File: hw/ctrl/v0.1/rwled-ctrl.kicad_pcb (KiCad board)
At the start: 2 copper layers, 70.9 x 38.1 mm, 49 parts, among them J21 batt-chg, J31 USB_B_Micro, J61 led-a, J62 led-b, J63 led-c, J64 led-d, J65 batt-ab, J66 batt-cd, Q31 UMH3N, Q61 IRF4905STRLPBF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

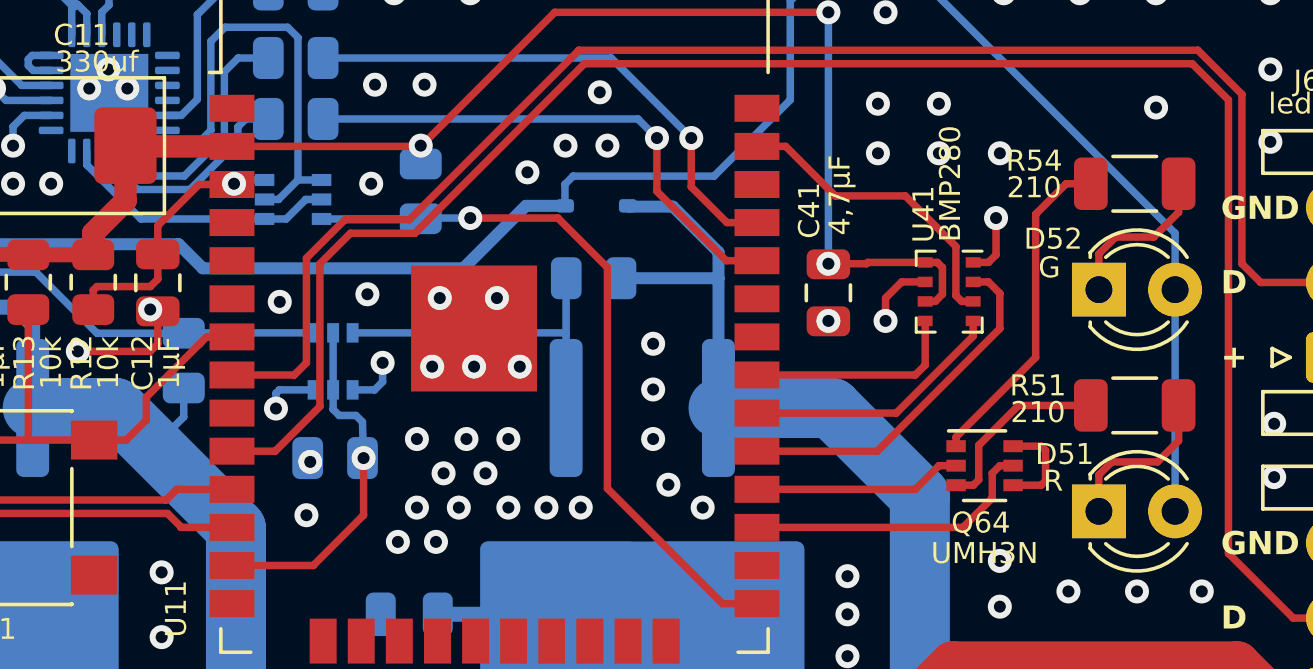
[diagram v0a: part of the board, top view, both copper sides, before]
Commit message: hw - архив доработанных и отправленных в заказ плат
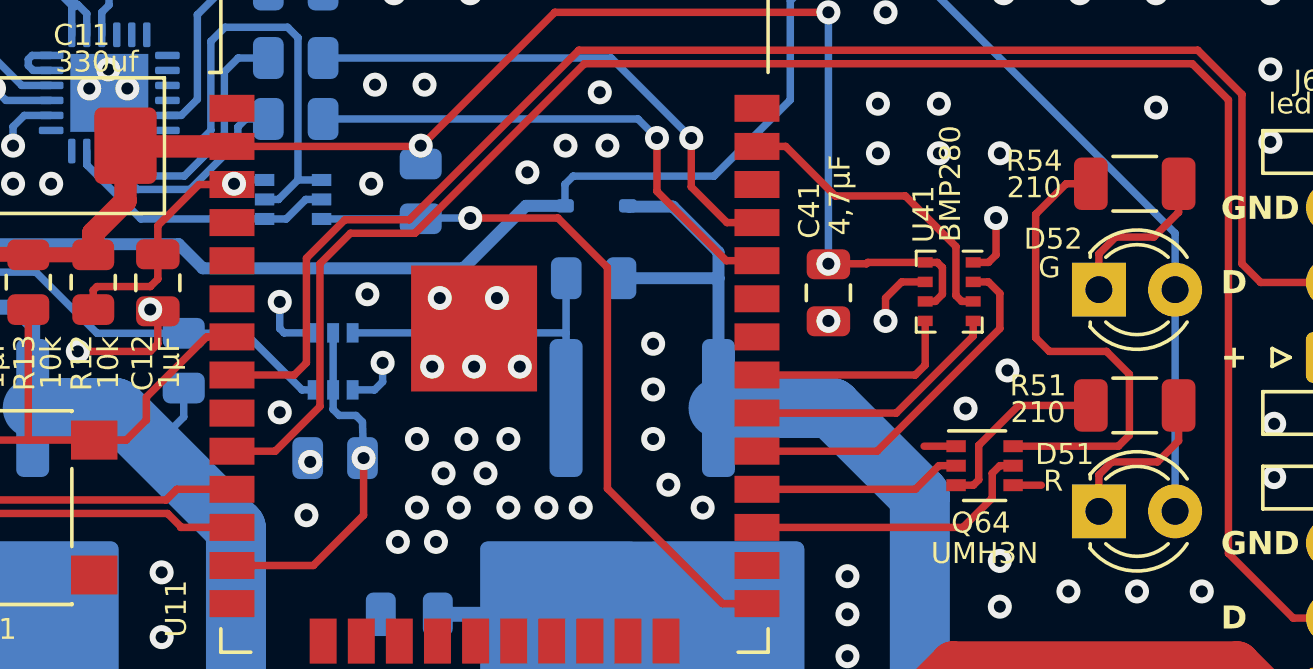
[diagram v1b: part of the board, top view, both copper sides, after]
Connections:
- Q63 pad 1: Net-(Q61-G) -> GND
- Q63 pad 6: GND -> Net-(Q61-G)
- Q64 pad 1: Net-(Q64A-E1) -> GND
- Q64 pad 6: GND -> Net-(Q64A-C1)
- R54 pad 1: Net-(Q64A-E1) -> Net-(Q64A-C1)
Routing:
- net Net-(Q64A-C1): track 0.00 -> 16.1 mm
- net Net-(Q64A-E1): track 11.1 -> 0.00 mm
- net GND: track 41.0 -> 40.0 mm, vias 156 -> 158
- net Net-(Q61-G): track 19.0 -> 19.8 mm
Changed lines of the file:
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@@
   (net 68 "unconnected-(U31-~{DCD}-Pad24)")
   (net 69 "Net-(Q62-G)")
-  (net 70 "Net-(Q64A-E1)")
+  (net 70 "Net-(Q64A-C1)")
   (net 71 "Net-(Q64B-C2)")
   (footprint "Resistor_SMD:R_0805_2012Metric" (layer "F.Cu")
@@
       (stroke (width 0.1) (type solid)) (layer "F.Fab"))
     (pad "1" smd rect (at -0.95 -0.65) (size 0.65 0.4) (layers "F.Cu" "F.Paste" "F.Mask")
-      (net 70 "Net-(Q64A-E1)") (pinfunction "E1") (pintype "passive"))
+      (net 2 "GND") (pinfunction "E1") (pintype "passive"))
     (pad "2" smd rect (at -0.95 0) (size 0.65 0.4) (layers "F.Cu" "F.Paste" "F.Mask")
       (net 30 "/led-g") (pinfunction "B1") (pintype "input"))
@@
       (net 29 "/led-r") (pinfunction "B2") (pintype "input"))
     (pad "6" smd rect (at 0.95 -0.65) (size 0.65 0.4) (layers "F.Cu" "F.Paste" "F.Mask")
-      (net 2 "GND") (pinfunction "C1") (pintype "passive"))
+      (net 70 "Net-(Q64A-C1)") (pinfunction "C1") (pintype "passive"))
     (model "${KICAD6_3DMODEL_DIR}/Package_TO_SOT_SMD.3dshapes/SOT-363_SC-70-6.wrl"
       (offset (xyz 0 0 0))
@@
       (stroke (width 0.1) (type solid)) (layer "F.Fab"))
     (pad "1" smd roundrect (at -1.4625 0) (size 1.125 1.75) (layers "F.Cu" "F.Paste" "F.Mask") (roundrect_rratio 0.2222222222)
-      (net 70 "Net-(Q64A-E1)") (pintype "passive"))
+      (net 70 "Net-(Q64A-C1)") (pintype "passive"))
     (pad "2" smd roundrect (at 1.4625 0) (size 1.125 1.75) (layers "F.Cu" "F.Paste" "F.Mask") (roundrect_rratio 0.2222222222)
       (net 10 "Net-(D52-K)") (pintype "passive"))
@@
       (stroke (width 0.1) (type solid)) (layer "B.Fab"))
     (pad "1" smd rect (at -0.95 0.65 270) (size 0.65 0.4) (layers "B.Cu" "B.Paste" "B.Mask")
-      (net 21 "Net-(Q61-G)") (pinfunction "E1") (pintype "passive"))
+      (net 2 "GND") (pinfunction "E1") (pintype "passive"))
     (pad "2" smd rect (at -0.95 0 270) (size 0.65 0.4) (layers "B.Cu" "B.Paste" "B.Mask")
       (net 31 "leden") (pinfunction "B1") (pintype "input"))
@@
       (net 31 "leden") (pinfunction "B2") (pintype "input"))
     (pad "6" smd rect (at 0.95 0.65 270) (size 0.65 0.4) (layers "B.Cu" "B.Paste" "B.Mask")
-      (net 2 "GND") (pinfunction "C1") (pintype "passive"))
+      (net 21 "Net-(Q61-G)") (pinfunction "C1") (pintype "passive"))
     (model "${KICAD6_3DMODEL_DIR}/Package_TO_SOT_SMD.3dshapes/SOT-363_SC-70-6.wrl"
       (offset (xyz 0 0 0))
@@
   (segment (start 128.016 57.404) (end 128.016 56.322) (width 0.25) (layer "F.Cu") (net 2))
   (segment (start 141.7104 76.835) (end 138.303 76.835) (width 1) (layer "F.Cu") (net 2))
-  (segment (start 157.607 60.96) (end 157.607 61.976) (width 0.25) (layer "F.Cu") (net 2))
   (segment (start 152.273 55.88) (end 152.273 56.642) (width 0.25) (layer "F.Cu") (net 2))
   (segment (start 155.194 54.692) (end 155.702 54.692) (width 0.25) (layer "F.Cu") (net 2))
-  (segment (start 157.607 61.976) (end 157.465 62.118) (width 0.25) (layer "F.Cu") (net 2))
   (segment (start 125.643 76.835) (end 122.555 76.835) (width 1) (layer "F.Cu") (net 2))
-  (segment (start 157.465 60.818) (end 157.607 60.96) (width 0.25) (layer "F.Cu") (net 2))
   (segment (start 115.738 46.134) (end 115.738 47.711) (width 0.4) (layer "F.Cu") (net 2))
   (segment (start 125.349 57.658) (end 127.762 57.658) (width 0.25) (layer "F.Cu") (net 2))
   (segment (start 155.956 53.213) (end 155.956 54.438) (width 0.25) (layer "F.Cu") (net 2))
   (segment (start 155.956 54.438) (end 155.702 54.692) (width 0.25) (layer "F.Cu") (net 2))
-  (segment (start 156.525 60.818) (end 157.465 60.818) (width 0.25) (layer "F.Cu") (net 2))
+  (segment (start 154.625 60.818) (end 153.558 60.818) (width 0.25) (layer "F.Cu") (net 2))
   (segment (start 152.811 55.342) (end 152.273 55.88) (width 0.25) (layer "F.Cu") (net 2))
   (segment (start 127.762 57.658) (end 128.016 57.404) (width 0.25) (layer "F.Cu") (net 2))
@@
   (via (at 153.67 77.47) (size 0.8) (drill 0.4) (layers "F.Cu" "B.Cu") (free) (net 2))
   (via (at 161.29 43.18) (size 0.8) (drill 0.4) (layers "F.Cu" "B.Cu") (free) (net 2))
+  (via (at 156.337 58.293) (size 0.8) (drill 0.4) (layers "F.Cu" "B.Cu") (free) (net 2))
   (via (at 136.906 48.768) (size 0.8) (drill 0.4) (layers "F.Cu" "B.Cu") (free) (net 2))
   (via (at 165.1 43.18) (size 0.8) (drill 0.4) (layers "F.Cu" "B.Cu") (free) (net 2))
@@
   (via (at 152.4 78.74) (size 0.8) (drill 0.4) (layers "F.Cu" "B.Cu") (free) (net 2))
   (via (at 134.62 77.47) (size 0.8) (drill 0.4) (layers "F.Cu" "B.Cu") (free) (net 2))
-  (via (at 131.953 59.563) (size 0.8) (drill 0.4) (layers "F.Cu" "B.Cu") (free) (net 2))
+  (via (at 132.08 59.69) (size 0.8) (drill 0.4) (layers "F.Cu" "B.Cu") (free) (net 2))
   (via (at 160.655 65.659) (size 0.8) (drill 0.4) (layers "F.Cu" "B.Cu") (free) (net 2))
   (via (at 107.95 50.8) (size 0.8) (drill 0.4) (layers "F.Cu" "B.Cu") (free) (net 2))
@@
   (via (at 165.1 48.26) (size 0.8) (drill 0.4) (layers "F.Cu" "B.Cu") (free) (net 2))
   (via (at 165.1 71.12) (size 0.8) (drill 0.4) (layers "F.Cu" "B.Cu") (free) (net 2))
+  (via (at 154.94 59.563) (size 0.8) (drill 0.4) (layers "F.Cu" "B.Cu") (free) (net 2))
   (via (at 137.287 64.008) (size 0.8) (drill 0.4) (layers "F.Cu" "B.Cu") (free) (net 2))
   (via (at 151.003 65.151) (size 0.8) (drill 0.4) (layers "F.Cu" "B.Cu") (free) (net 2))
@@
   (segment (start 141.7104 76.835) (end 138.303 76.835) (width 1) (layer "B.Cu") (net 2))
   (segment (start 123.563 49.792) (end 123.19 50.165) (width 0.25) (layer "B.Cu") (net 2))
-  (segment (start 131.953 59.563) (end 131.953 59.055) (width 0.25) (layer "B.Cu") (net 2))
   (segment (start 123.19 50.165) (end 123.19 50.8) (width 0.25) (layer "B.Cu") (net 2))
   (segment (start 124.46 49.792) (end 123.563 49.792) (width 0.25) (layer "B.Cu") (net 2))
+  (segment (start 132.08 56.007) (end 132.08 56.896) (width 0.25) (layer "B.Cu") (net 2))
   (segment (start 157.774 76.835) (end 154.559 76.835) (width 1) (layer "B.Cu") (net 2))
-  (segment (start 133.208 58.9405) (end 132.0675 58.9405) (width 0.25) (layer "B.Cu") (net 2))
   (segment (start 135.509 58.674) (end 135.509 58.039) (width 0.25) (layer "B.Cu") (net 2))
-  (segment (start 132.0675 58.9405) (end 131.953 59.055) (width 0.25) (layer "B.Cu") (net 2))
+  (segment (start 132.2245 57.0405) (end 133.208 57.0405) (width 0.25) (layer "B.Cu") (net 2))
+  (segment (start 132.08 56.896) (end 132.2245 57.0405) (width 0.25) (layer "B.Cu") (net 2))
   (segment (start 125.643 76.835) (end 121.92 76.835) (width 1) (layer "B.Cu") (net 2))
   (segment (start 134.508 58.9405) (end 135.2425 58.9405) (width 0.25) (layer "B.Cu") (net 2))
@@
   (segment (start 118.764 59.545) (end 118.764 56.3436) (width 0.25) (layer "B.Cu") (net 21))
   (segment (start 120.0912 55.0164) (end 123.952 55.0164) (width 0.25) (layer "B.Cu") (net 21))
-  (segment (start 133.208 57.0405) (end 128.8936 57.0405) (width 0.25) (layer "B.Cu") (net 21))
+  (segment (start 128.8796 57.0545) (end 130.937 57.0545) (width 0.25) (layer "B.Cu") (net 21))
   (segment (start 128.8796 57.0545) (end 125.9901 57.0545) (width 0.25) (layer "B.Cu") (net 21))
   (segment (start 118.764 56.3436) (end 120.0912 55.0164) (width 0.25) (layer "B.Cu") (net 21))
   (segment (start 125.9901 57.0545) (end 123.952 55.0164) (width 0.25) (layer "B.Cu") (net 21))
+  (segment (start 130.937 57.0545) (end 132.823 58.9405) (width 0.25) (layer "B.Cu") (net 21))
+  (segment (start 132.823 58.9405) (end 133.208 58.9405) (width 0.25) (layer "B.Cu") (net 21))
   (segment (start 127.635 59.182) (end 129.642 57.175) (width 0.25) (layer "F.Cu") (net 22))
   (segment (start 127.635 59.944) (end 127.635 59.182) (width 0.25) (layer "F.Cu") (net 22))
@@
   (segment (start 134.508 57.0405) (end 141.6161 57.0405) (width 0.25) (layer "B.Cu") (net 69))
   (segment (start 141.6161 57.0405) (end 141.624 57.0484) (width 0.25) (layer "B.Cu") (net 69))
-  (segment (start 154.625 60.513) (end 157.2768 57.8612) (width 0.25) (layer "F.Cu") (net 70))
-  (segment (start 157.2768 53.086) (end 158.2928 52.07) (width 0.25) (layer "F.Cu") (net 70))
-  (segment (start 158.2928 52.07) (end 159.1163 52.07) (width 0.25) (layer "F.Cu") (net 70))
-  (segment (start 157.2768 57.8612) (end 157.2768 53.086) (width 0.25) (layer "F.Cu") (net 70))
-  (segment (start 154.625 60.818) (end 154.625 60.513) (width 0.25) (layer "F.Cu") (net 70))
+  (segment (start 159.1163 52.07) (end 158.2928 52.07) (width 0.25) (layer "F.Cu") (net 70))
+  (segment (start 157.2768 57.2008) (end 157.734 57.658) (width 0.25) (layer "F.Cu") (net 70))
+  (segment (start 160.035 60.818) (end 156.525 60.818) (width 0.25) (layer "F.Cu") (net 70))
+  (segment (start 160.401 60.452) (end 160.035 60.818) (width 0.25) (layer "F.Cu") (net 70))
+  (segment (start 157.2768 53.086) (end 157.2768 57.2008) (width 0.25) (layer "F.Cu") (net 70))
+  (segment (start 158.2928 52.07) (end 157.2768 53.086) (width 0.25) (layer "F.Cu") (net 70))
+  (segment (start 157.734 57.658) (end 159.639 57.658) (width 0.25) (layer "F.Cu") (net 70))
+  (segment (start 160.401 58.42) (end 160.401 60.452) (width 0.25) (layer "F.Cu") (net 70))
+  (segment (start 159.639 57.658) (end 160.401 58.42) (width 0.25) (layer "F.Cu") (net 70))
   (segment (start 156.7085 59.4595) (end 159.1163 59.4595) (width 0.25) (layer "F.Cu") (net 71))
   (segment (start 154.625 62.118) (end 155.2 62.118) (width 0.25) (layer "F.Cu") (net 71))
